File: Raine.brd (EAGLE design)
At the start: 307.5 x 100.4 mm, 171 parts, among them J1 USB-C-M12-TYPE-C-31-M12, SW1 TL3342F160QG/TR, U2 ATMEGA32U4-AUR44ML-L

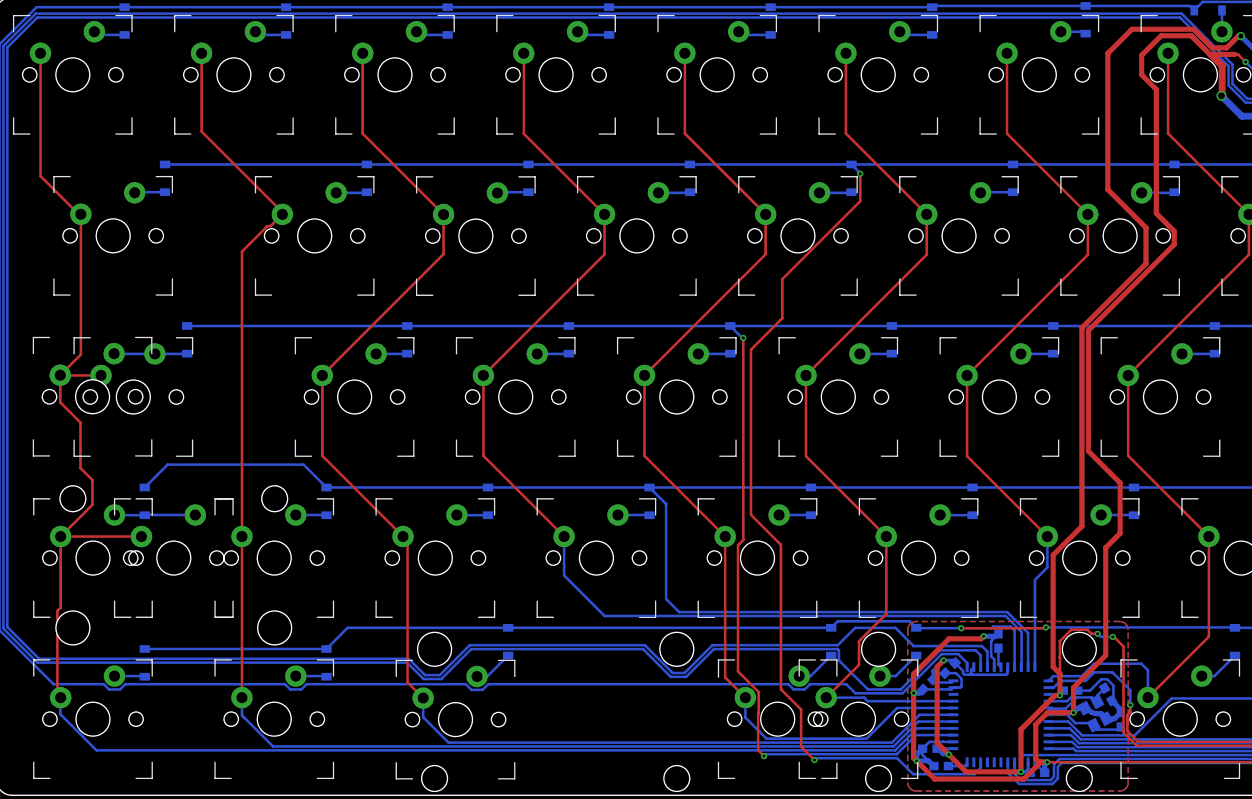
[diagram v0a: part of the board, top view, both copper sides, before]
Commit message: minor trace moves
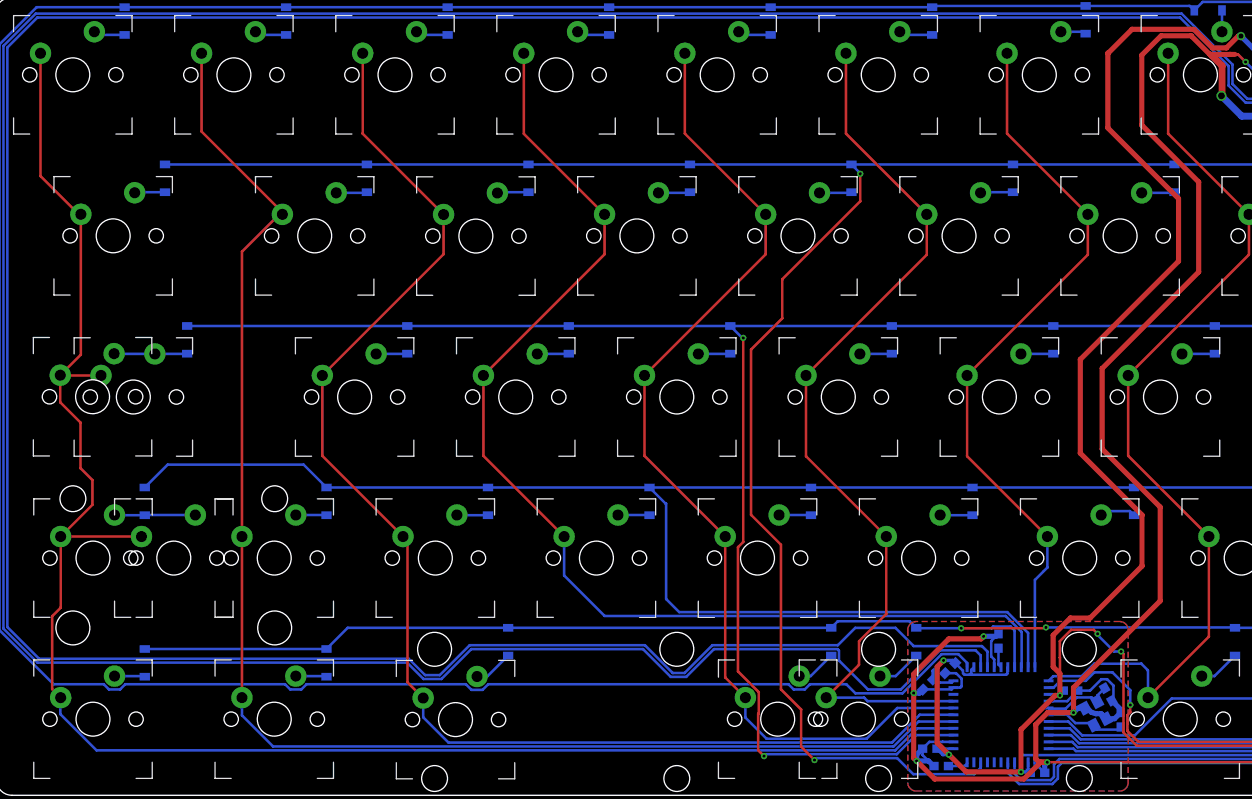
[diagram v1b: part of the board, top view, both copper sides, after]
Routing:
- net +5V: track 240.0 -> 250.2 mm
- net GND: track 314.3 -> 319.3 mm
- net COL01: track 207.1 -> 207.6 mm

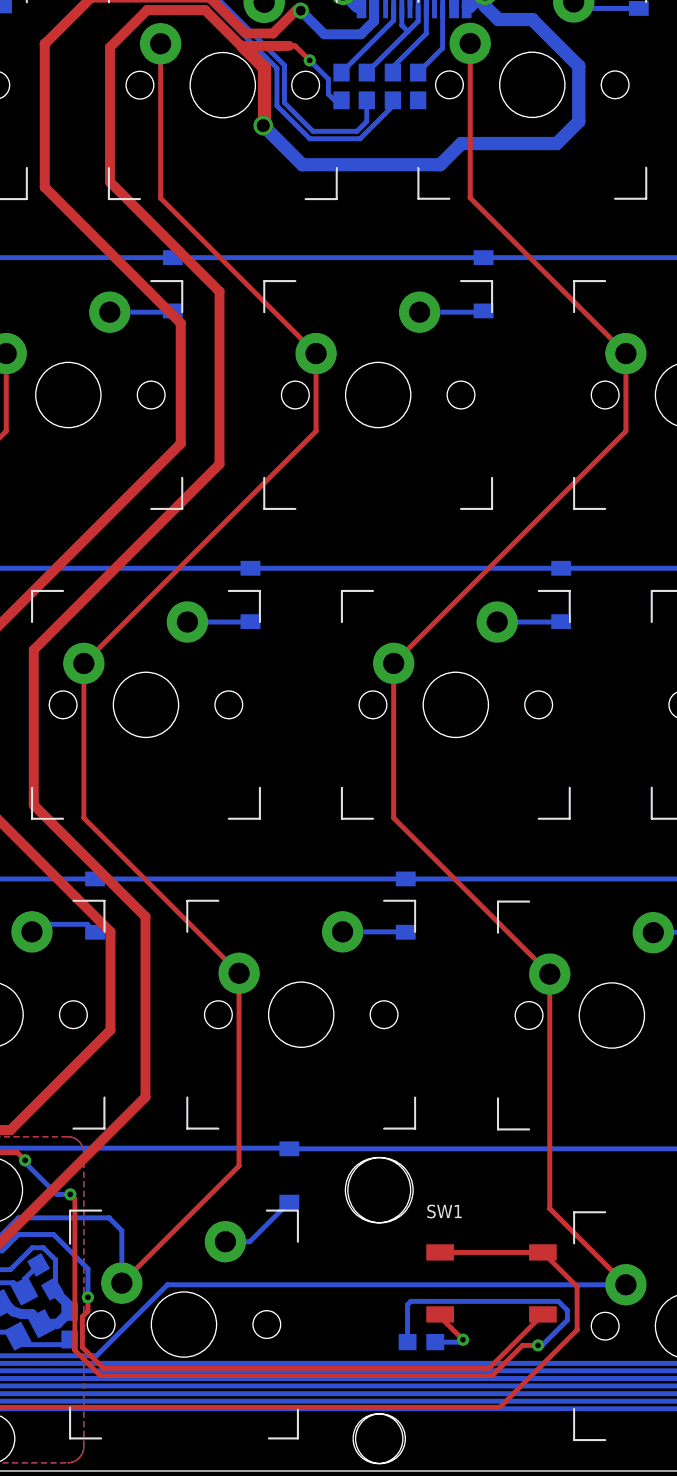
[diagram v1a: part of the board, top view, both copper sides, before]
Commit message: Add reset switch to bottom of pcb
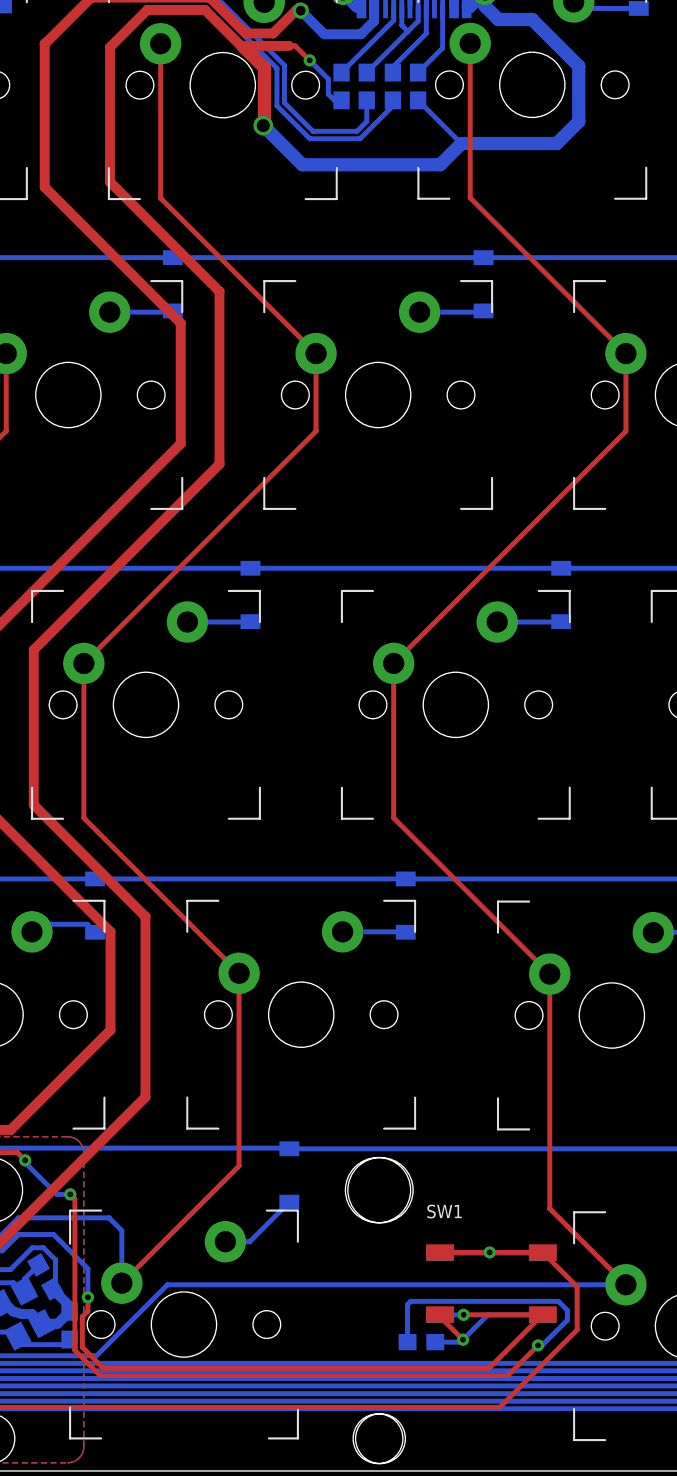
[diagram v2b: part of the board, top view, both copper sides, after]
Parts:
- added SW2: TL3342F160QG/TR, Keyboard_parts:SW_TL3342F160QG/TR
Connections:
- net GND: now also SW2.3, SW2.4
- net N$89: now also SW2.1
- net RST: now also SW2.2
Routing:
- net GND: track 319.3 -> 329.8 mm, vias 7 -> 8
- net RST: track 46.3 -> 52.7 mm, vias 1 -> 2
- net N$89: track 3.89 -> 9.40 mm
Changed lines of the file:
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@@
 <attribute name="VALUE" x="152.80723125" y="-11.262440625" size="0.6008875" layer="28" rot="MR270"/>
+</element>
+<element name="SW2" library="Keyboard_parts" library_urn="urn:adsk.eagle:library:6380734" package="SW_TL3342F160QG/TR" package3d_urn="urn:adsk.eagle:package:6174039/2" value="TL3342F160QG/TR" x="158.984" y="-83.032" smashed="yes" rot="MR0">
+<attribute name="DESCRIPTION" value=" Switch Tactile Spst-No 0.05a 12v " x="167.616" y="-72.328" size="1.778" layer="28" rot="MR0" display="off"/>
+<attribute name="DIGI-KEY_PART_NUMBER" value="EG2531CT-ND" x="167.616" y="-72.328" size="1.778" layer="28" rot="MR0" display="off"/>
+<attribute name="DIGI-KEY_PURCHASE_URL" value="https://www.digikey.co.uk/product-detail/en/e-switch/TL3342F160QG-TR/EG2531CT-ND/379004?utm_source=snapeda&amp;utm_medium=aggregator&amp;utm_campaign=symbol" x="167.616" y="-72.328" size="1.778" layer="28" rot="MR0" display="off"/>
+<attribute name="MF" value="E-Switch" x="167.616" y="-72.328" size="1.778" layer="28" rot="MR0" display="off"/>
+<attribute name="MP" value="TL3342F160QG/TR" x="167.616" y="-72.328" size="1.778" layer="28" rot="MR0" display="off"/>
+<attribute name="NAME" x="162.988890625" y="-79.027109375" size="0.81379375" layer="26" rot="MR0"/>
+<attribute name="PACKAGE" value="FakePackage u" x="167.616" y="-72.328" size="1.778" layer="28" rot="MR0" display="off"/>
+<attribute name="VALUE" x="162.992159375" y="-88.0422" size="0.814459375" layer="28" rot="MR0"/>
 </element>
 </elements>
@@
 <contactref element="CR1" pad="4"/>
 <contactref element="SW1" pad="3"/>
-<contactref element="SW1" pad="4"/>
 <contactref element="C4" pad="2"/>
 <contactref element="C8" pad="2"/>
@@
 <wire x1="147.85" y1="-8" x2="148.9952" y2="-9.1452" width="0.3048" layer="16"/>
 <wire x1="148.9952" y1="-9.1452" x2="148.9952" y2="-10.07625" width="0.3048" layer="16"/>
-<wire x1="149.36895" y1="-10.45" x2="148.9952" y2="-10.07625" width="0.3048" layer="16"/>
-<wire x1="155.85" y1="-81.1" x2="162.15" y2="-81.1" width="0.3048" layer="1"/>
-<wire x1="162.15" y1="-81.1" x2="164.25" y2="-83.2" width="0.3048" layer="1"/>
 <wire x1="164.25" y1="-83.2" x2="164.25" y2="-85.85" width="0.3048" layer="1"/>
 <wire x1="164.25" y1="-85.85" x2="159.5" y2="-90.6" width="0.3048" layer="1"/>
@@
 <contactref element="R3" pad="2"/>
 <contactref element="R4" pad="2"/>
-<wire x1="149.8" y1="-10.45" x2="154.5" y2="-10.45" width="0" layer="19" extent="16-16"/>
-<wire x1="149.36895" y1="-10.45" x2="149.8" y2="-10.45" width="0" layer="19" extent="16-16"/>
+<contactref element="SW2" pad="3"/>
+<contactref element="SW1" pad="4"/>
+<contactref element="SW2" pad="4"/>
+<wire x1="164.25" y1="-83.2" x2="162.15" y2="-81.1" width="0.3048" layer="1"/>
+<wire x1="162.15" y1="-81.1" x2="158.888" y2="-81.1" width="0.3048" layer="1"/>
+<wire x1="158.888" y1="-81.1" x2="155.85" y2="-81.1" width="0.3048" layer="1"/>
+<wire x1="155.834" y1="-81.132" x2="158.888" y2="-81.132" width="0.3048" layer="16"/>
+<wire x1="158.888" y1="-81.132" x2="162.134" y2="-81.132" width="0.3048" layer="16"/>
+<wire x1="158.888" y1="-81.132" x2="158.888" y2="-81.1" width="0.3048" layer="16"/>
+<via x="158.888" y="-81.1" extent="1-16" drill="0.35"/>
+<wire x1="149.8" y1="-10.45" x2="149.36895" y2="-10.45" width="0.3048" layer="16"/>
+<wire x1="149.36895" y1="-10.45" x2="148.9952" y2="-10.07625" width="0.3048" layer="16"/>
+<wire x1="154.5" y1="-10.45" x2="157.15" y2="-13.1" width="0.3048" layer="16"/>
 </signal>
 <signal name="+5V" airwireshidden="yes">
@@
 <wire x1="162.1" y1="-86.8" x2="161.85" y2="-86.8" width="0.3048" layer="16"/>
 <via x="161.85" y="-86.8" extent="1-16" drill="0.35"/>
-<wire x1="161.85" y1="-86.8" x2="160.89658125" y2="-86.8" width="0.3048" layer="1"/>
-<wire x1="160.89658125" y1="-86.8" x2="159.03938125" y2="-88.6572" width="0.3048" layer="1"/>
-<wire x1="159.03938125" y1="-88.6572" x2="135.01061875" y2="-88.6572" width="0.3048" layer="1"/>
+<wire x1="161.85" y1="-86.8" x2="159.9928" y2="-88.6572" width="0.3048" layer="1"/>
+<wire x1="159.9928" y1="-88.6572" x2="135.01061875" y2="-88.6572" width="0.3048" layer="1"/>
 <wire x1="135.01061875" y1="-88.6572" x2="133.448" y2="-87.09458125" width="0.3048" layer="1"/>
 <wire x1="154.05" y1="-84.1" x2="163.1" y2="-84.1" width="0.3048" layer="16"/>
@@
 <wire x1="133.9052" y1="-86.9052" x2="135.2" y2="-88.2" width="0.3048" layer="1"/>
 <wire x1="135.2" y1="-88.2" x2="158.85" y2="-88.2" width="0.3048" layer="1"/>
+<contactref element="SW2" pad="2"/>
+<wire x1="155.834" y1="-84.932" x2="157.276" y2="-84.932" width="0.3048" layer="16"/>
+<wire x1="157.276" y1="-84.932" x2="157.288" y2="-84.92" width="0.3048" layer="16"/>
+<via x="157.288" y="-84.92" extent="1-16" drill="0.35"/>
+<wire x1="157.288" y1="-84.92" x2="162.13" y2="-84.92" width="0.3048" layer="1"/>
+<wire x1="162.13" y1="-84.92" x2="162.15" y2="-84.9" width="0.3048" layer="1"/>
 </signal>
 <signal name="COL01" airwireshidden="yes">
@@
 <wire x1="157.25" y1="-86.45" x2="155.85" y2="-85.05" width="0.3048" layer="1"/>
 <wire x1="155.85" y1="-85.05" x2="155.85" y2="-84.9" width="0.3048" layer="1"/>
+<contactref element="SW2" pad="1"/>
+<wire x1="157.25" y1="-86.45" x2="158.768" y2="-84.932" width="0.3048" layer="16"/>
+<wire x1="158.768" y1="-84.932" x2="162.134" y2="-84.932" width="0.3048" layer="16"/>
 </signal>
 <signal name="N$1" airwireshidden="yes">
